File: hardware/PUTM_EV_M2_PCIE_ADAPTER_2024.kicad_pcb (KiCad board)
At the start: 4 copper layers, 80 x 22 mm, 13 parts, among them J1 PCIE-064-02-X-D-RA, J2 M2_KEY_M, J3 PCB_WIRE

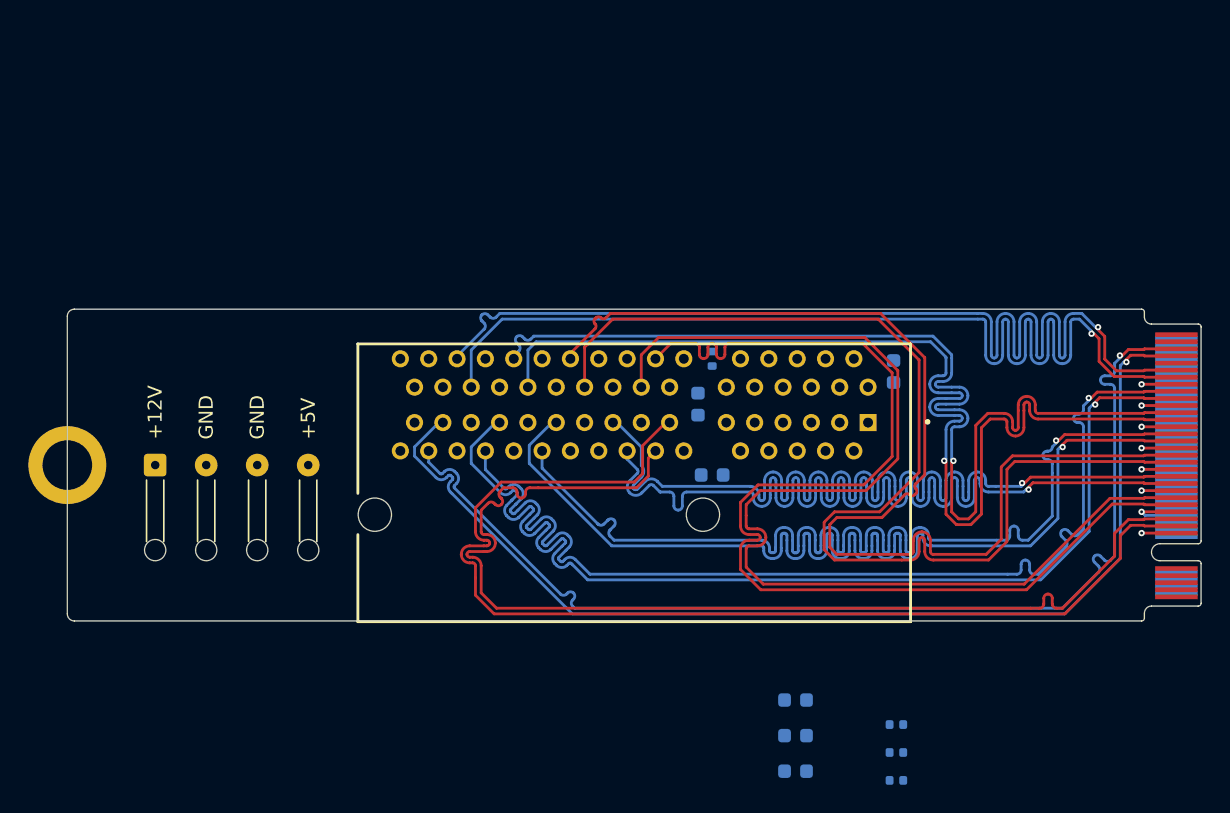
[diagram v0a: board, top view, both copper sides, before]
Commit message: deleted all tracks, needs a bigger board
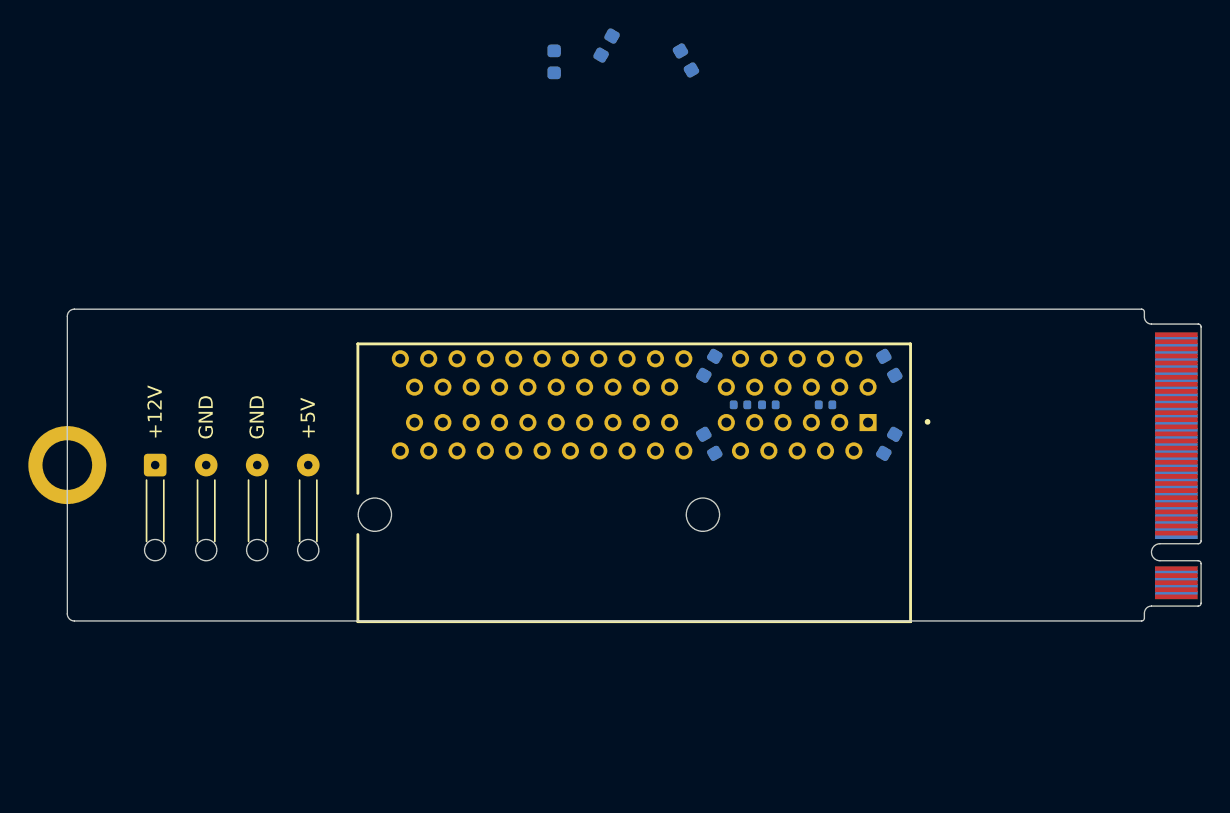
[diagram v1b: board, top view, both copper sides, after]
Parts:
- removed R1: 0, Resistor_SMD:R_0402_1005Metric
- added C10: 1uF, Capacitor_SMD:C_0603_1608Metric, B.Cu at (173.0, 111.5)
- moved C4 50.5 mm to (153.1, 83.4), turned to -120 degrees
- moved C6 29.2 mm to (160.3, 106.0), turned to -120 degrees
- moved C5 28.7 mm to (162.5, 108.8)
- moved C8 26.4 mm to (158.7, 84.5), turned to 120 degrees
- moved C9 26.2 mm to (149.3, 84.5)
- moved C3 26.1 mm to (164.5, 108.8), turned to 0 degrees
- moved C2 24.5 mm to (173.0, 106.0), turned to 120 degrees
- moved C1 23.1 mm to (168.5, 108.8)
- moved C7 2.21 mm to (160.3, 111.5), turned to 120 degrees
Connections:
- C5 pad 1: /+3.3AUX -> +3.3V
- C6 pad 1: /+3.3AUX -> +3.3V
- J1 pad B10: /+3.3AUX -> +3.3V
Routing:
- net /REFCLK+: track 80.0 -> 0.00 mm
- net /DO1+: track 79.9 -> 0.00 mm
- net /DO0-: track 79.9 -> 0.00 mm
- net /DO1-: track 79.9 -> 0.00 mm
- net /DO0+: track 79.8 -> 0.00 mm
- net /REFCLK-: track 79.8 -> 0.00 mm
- net /DI3+: track 78.5 -> 0.00 mm, vias 1 -> 0
- net /DI2+: track 78.3 -> 0.00 mm, vias 1 -> 0
- net /DI3-: track 78.3 -> 0.00 mm, vias 1 -> 0
- net /DO3+: track 78.2 -> 0.00 mm, vias 1 -> 0
- net /DO2+: track 78.2 -> 0.00 mm, vias 1 -> 0
- net /DO3-: track 78.2 -> 0.00 mm, vias 1 -> 0
- net /DO2-: track 78.2 -> 0.00 mm, vias 1 -> 0
- net /DI1+: track 78.1 -> 0.00 mm, vias 1 -> 0
- net /DI2-: track 78.1 -> 0.00 mm, vias 1 -> 0
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
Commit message: final design
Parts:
- J2: footprint Snapeda:M.2-KEY-M -> Snapeda:M.2-KEY-M-FAT
- moved C4 33.0 mm to (165.5, 114.0), turned to 0 degrees
- moved C9 32.2 mm to (165.5, 112.4), turned to 0 degrees
- moved C8 31.9 mm to (165.5, 115.6), turned to 0 degrees
- moved C2 4.88 mm to (169.5, 102.6), turned to 180 degrees
- moved C6 4.67 mm to (163.5, 102.6), turned to 0 degrees
- moved C10 3.61 mm to (169.5, 112.4), turned to 180 degrees
- moved C7 2.38 mm to (162.5, 112.4), turned to 180 degrees
- moved C1 1.25 mm to (168.5, 107.5)
- moved C3 1.25 mm to (164.5, 107.5)
- moved C5 1.25 mm to (162.5, 107.5)
- moved J1 1.25 mm to (155.0, 113.0)
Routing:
- net /DI3+: track 0.00 -> 69.9 mm
- net /DI3-: track 0.00 -> 69.7 mm
- net /DI2+: track 0.00 -> 69.2 mm, vias 0 -> 1
- net /DI1+: track 0.00 -> 69.2 mm, vias 0 -> 1
- net /REFCLK+: track 0.00 -> 69.1 mm, vias 0 -> 1
- net /DI2-: track 0.00 -> 69.0 mm, vias 0 -> 1
- net /DI1-: track 0.00 -> 69.0 mm, vias 0 -> 1
- net /REFCLK-: track 0.00 -> 69.0 mm, vias 0 -> 1
- net /DO3+: track 0.00 -> 68.9 mm, vias 0 -> 1
- net /DO3-: track 0.00 -> 68.9 mm, vias 0 -> 1
- net /DO1+: track 0.00 -> 68.4 mm, vias 0 -> 2
- net /DI0-: track 0.00 -> 68.4 mm, vias 0 -> 2
- net /DO1-: track 0.00 -> 68.3 mm, vias 0 -> 2
- net /DO0-: track 0.00 -> 68.3 mm, vias 0 -> 2
- net /DI0+: track 0.00 -> 68.3 mm, vias 0 -> 2
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- added copper zone on F.Cu, net +12V
- added copper zone on B.Cu, net +3.3V
- added copper zone on F.Cu, net +3.3V
- added copper zone on F.Cu, net GND
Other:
- board size 80 x 22 mm -> 80 x 32 mm
